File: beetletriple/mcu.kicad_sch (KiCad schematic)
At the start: 14 parts, among them J5 input_c1, J6 input_c2, J7 input_c3, U3 ATtiny1617-M

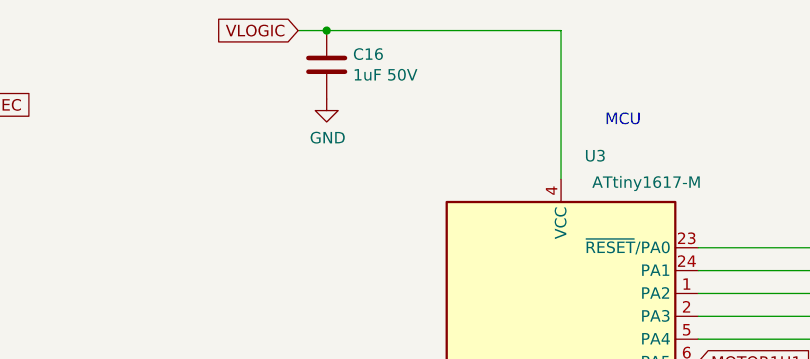
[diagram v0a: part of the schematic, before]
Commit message: Beetleweight triple esc
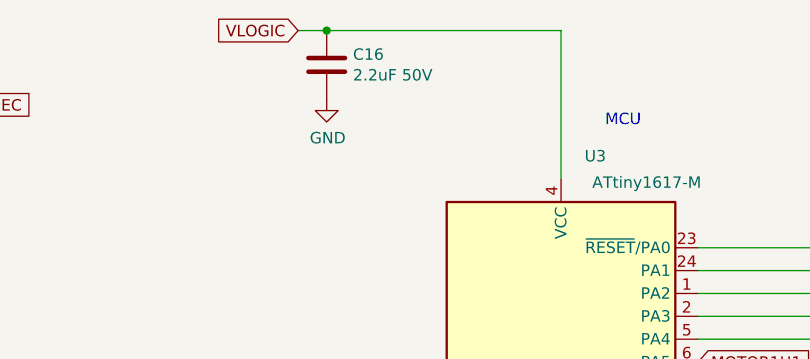
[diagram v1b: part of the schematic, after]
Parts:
- C16: value 1uF 50V -> 2.2uF 50V; LCSC (none) -> C50254
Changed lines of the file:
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@@
       (effects (font (size 1.27 1.27)) (justify left))
     )
-    (property "Value" "1uF 50V" (id 1) (at 106.4261 62.1093 0)
+    (property "Value" "2.2uF 50V" (id 1) (at 106.4261 62.1093 0)
       (effects (font (size 1.27 1.27)) (justify left))
     )
@@
       (effects (font (size 1.27 1.27)) hide)
     )
-    (property "LCSC" "" (id 4) (at 103.505 60.96 0)
+    (property "LCSC" "C50254" (id 4) (at 103.505 60.96 0)
       (effects (font (size 1.27 1.27)) hide)
     )

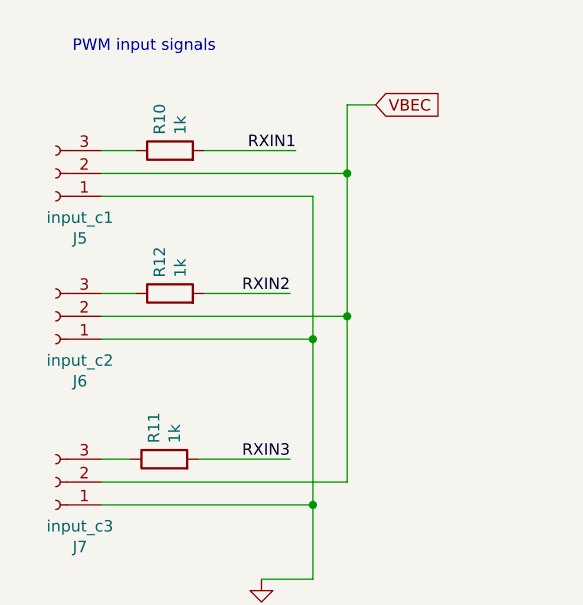
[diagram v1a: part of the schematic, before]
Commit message: Beetleweight triple: redo the power and passives
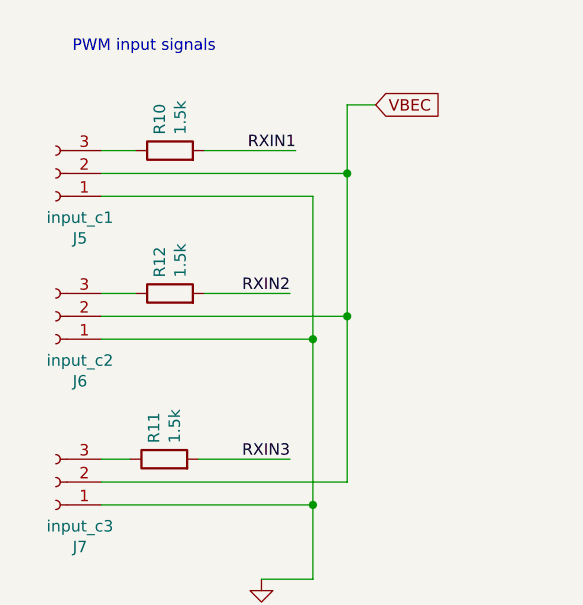
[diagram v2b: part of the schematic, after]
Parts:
- R10, R11, R12: value 1k -> 1.5k
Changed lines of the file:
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@@
       (effects (font (size 1.27 1.27)) (justify left))
     )
-    (property "Value" "1k" (id 1) (at 41.154 102.997 0)
+    (property "Value" "1.5k" (id 1) (at 41.154 102.997 0)
       (effects (font (size 1.27 1.27)) (justify left))
     )
@@
       (effects (font (size 1.27 1.27)) (justify left))
     )
-    (property "Value" "1k" (id 1) (at 41.789 68.707 0)
+    (property "Value" "1.5k" (id 1) (at 41.789 68.707 0)
       (effects (font (size 1.27 1.27)) (justify left))
     )
@@
       (effects (font (size 1.27 1.27)) (justify left))
     )
-    (property "Value" "1k" (id 1) (at 41.789 84.582 0)
+    (property "Value" "1.5k" (id 1) (at 41.789 84.582 0)
       (effects (font (size 1.27 1.27)) (justify left))
     )

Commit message: Beetleweight triple: more.
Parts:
- added J8: output_c4, Connector_PinHeader_2.54mm:PinHeader_1x03_P2.54mm_Vertical, symbol Connector:Conn_01x03_Female
- added J9: output_c5, Connector_PinHeader_2.54mm:PinHeader_1x03_P2.54mm_Vertical, symbol Connector:Conn_01x03_Female
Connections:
- net GND: now also J8.1 (Pin_1), J9.1 (Pin_1)
- net MOTOR1H1: now also U3.11 (PB5); no longer U3.6 (PA5)
- net MOTOR1H2: now also U3.9 (PB7); no longer U3.8 (PA7)
- net MOTOR1L1: now also U3.10 (PB6); no longer U3.7 (PA6)
- net MOTOR1L2: now also U3.8 (PA7); no longer U3.16 (PB0)
- net MOTOR2H1: now also U3.17 (PC0); no longer U3.15 (PB1)
- net MOTOR2H2: now also U3.7 (PA6); no longer U3.13 (PB3)
- net MOTOR2L1: now also U3.16 (PB0); no longer U3.14 (PB2)
- net MOTOR2L2: now also U3.6 (PA5); no longer U3.12 (PB4)
- net MOTOR3H1: now also U3.15 (PB1); no longer U3.11 (PB5)
- net MOTOR3H2: now also U3.13 (PB3); no longer U3.9 (PB7)
- net MOTOR3L1: now also U3.14 (PB2); no longer U3.10 (PB6)
- net MOTOR3L2: now also U3.12 (PB4); no longer U3.17 (PC0)
- net VBEC: now also J8.2 (Pin_2), J9.2 (Pin_2)
- net SERVO2: now reaches U3.19 (PC2)
- net SERVO2: now also J9.3 (Pin_3)
- net SERVO1: now reaches U3.20 (PC3)
- net SERVO1: now also J8.3 (Pin_3)
- no-connect marks 0 -> 1
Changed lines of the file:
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@@
   (junction (at 95.885 168.275) (diameter 0.9144) (color 0 0 0 0))
   (junction (at 103.505 57.15) (diameter 0.9144) (color 0 0 0 0))
+  (junction (at 220.345 116.84) (diameter 0.9144) (color 0 0 0 0))
+  (junction (at 225.425 98.425) (diameter 0.9144) (color 0 0 0 0))
+  (no_connect (at 114.3 106.68))
   (wire (pts (xy 33.02 70.485) (xy 36.83 70.485))
     (stroke (width 0) (type solid) (color 0 0 0 0))
@@
     (stroke (width 0) (type solid) (color 0 0 0 0))
   )
+  (wire (pts (xy 104.14 109.22) (xy 114.3 109.22))
+    (stroke (width 0) (type solid) (color 0 0 0 0))
+  )
+  (wire (pts (xy 104.14 111.76) (xy 114.3 111.76))
+    (stroke (width 0) (type solid) (color 0 0 0 0))
+  )
   (wire (pts (xy 108.585 132.715) (xy 108.585 146.685))
     (stroke (width 0) (type solid) (color 0 0 0 0))
@@
     (stroke (width 0) (type solid) (color 0 0 0 0))
   )
+  (wire (pts (xy 220.345 100.965) (xy 220.345 116.84))
+    (stroke (width 0) (type solid) (color 0 0 0 0))
+  )
+  (wire (pts (xy 220.345 116.84) (xy 220.345 123.19))
+    (stroke (width 0) (type solid) (color 0 0 0 0))
+  )
+  (wire (pts (xy 220.345 116.84) (xy 236.855 116.84))
+    (stroke (width 0) (type solid) (color 0 0 0 0))
+  )
+  (wire (pts (xy 225.425 70.485) (xy 218.44 70.485))
+    (stroke (width 0) (type solid) (color 0 0 0 0))
+  )
+  (wire (pts (xy 225.425 70.485) (xy 225.425 98.425))
+    (stroke (width 0) (type solid) (color 0 0 0 0))
+  )
+  (wire (pts (xy 225.425 98.425) (xy 225.425 114.3))
+    (stroke (width 0) (type solid) (color 0 0 0 0))
+  )
+  (wire (pts (xy 226.695 95.885) (xy 236.855 95.885))
+    (stroke (width 0) (type solid) (color 0 0 0 0))
+  )
+  (wire (pts (xy 228.6 111.76) (xy 236.855 111.76))
+    (stroke (width 0) (type solid) (color 0 0 0 0))
+  )
+  (wire (pts (xy 236.855 98.425) (xy 225.425 98.425))
+    (stroke (width 0) (type solid) (color 0 0 0 0))
+  )
+  (wire (pts (xy 236.855 100.965) (xy 220.345 100.965))
+    (stroke (width 0) (type solid) (color 0 0 0 0))
+  )
+  (wire (pts (xy 236.855 114.3) (xy 225.425 114.3))
+    (stroke (width 0) (type solid) (color 0 0 0 0))
+  )
   (text "PWM input signals" (at 45.72 59.69 180)
     (effects (font (size 1.27 1.27)) (justify right bottom))
@@
     (effects (font (size 1.27 1.27)) (justify left bottom))
   )
+  (label "SERVO2" (at 104.14 109.22 0)
+    (effects (font (size 1.27 1.27)) (justify left bottom))
+  )
+  (label "SERVO1" (at 104.14 111.76 0)
+    (effects (font (size 1.27 1.27)) (justify left bottom))
+  )
   (label "BLINKY2" (at 108.585 144.78 90)
     (effects (font (size 1.27 1.27)) (justify left bottom))
@@
   (label "RXIN3" (at 165.735 91.44 180)
     (effects (font (size 1.27 1.27)) (justify right bottom))
+  )
+  (label "SERVO1" (at 226.695 95.885 0)
+    (effects (font (size 1.27 1.27)) (justify left bottom))
+  )
+  (label "SERVO2" (at 228.6 111.76 0)
+    (effects (font (size 1.27 1.27)) (justify left bottom))
   )
   (global_label "VBEC" (shape input) (at 63.5 65.405 0)
@@
     )
   )
-  (global_label "MOTOR3L2" (shape input) (at 114.3 104.14 180)
+  (global_label "MOTOR2H1" (shape input) (at 114.3 104.14 180)
     (effects (font (size 1.27 1.27)) (justify right))
-    (property "Intersheet References" "${INTERSHEET_REFS}" (id 0) (at 100.5658 104.0606 0)
+    (property "Intersheet References" "${INTERSHEET_REFS}" (id 0) (at 100.2634 104.2194 0)
       (effects (font (size 1.27 1.27)) (justify right) hide)
     )
   )
-  (global_label "MOTOR1H1" (shape input) (at 144.78 93.98 0)
-    (effects (font (size 1.27 1.27)) (justify left))
-    (property "Intersheet References" "${INTERSHEET_REFS}" (id 0) (at 158.8166 93.9006 0)
-      (effects (font (size 1.27 1.27)) (justify left) hide)
-    )
-  )
-  (global_label "MOTOR1L1" (shape input) (at 144.78 96.52 0)
-    (effects (font (size 1.27 1.27)) (justify left))
-    (property "Intersheet References" "${INTERSHEET_REFS}" (id 0) (at 158.5142 96.4406 0)
-      (effects (font (size 1.27 1.27)) (justify left) hide)
-    )
-  )
-  (global_label "MOTOR1H2" (shape input) (at 144.78 99.06 0)
-    (effects (font (size 1.27 1.27)) (justify left))
-    (property "Intersheet References" "${INTERSHEET_REFS}" (id 0) (at 158.8166 98.9806 0)
-      (effects (font (size 1.27 1.27)) (justify left) hide)
-    )
-  )
-  (global_label "MOTOR1L2" (shape input) (at 144.78 104.14 0)
+  (global_label "MOTOR2L2" (shape input) (at 144.78 93.98 0)
+    (effects (font (size 1.27 1.27)) (justify left))
+    (property "Intersheet References" "${INTERSHEET_REFS}" (id 0) (at 158.5142 93.9006 0)
+      (effects (font (size 1.27 1.27)) (justify left) hide)
+    )
+  )
+  (global_label "MOTOR2H2" (shape input) (at 144.78 96.52 0)
+    (effects (font (size 1.27 1.27)) (justify left))
+    (property "Intersheet References" "${INTERSHEET_REFS}" (id 0) (at 158.8166 96.4406 0)
+      (effects (font (size 1.27 1.27)) (justify left) hide)
+    )
+  )
+  (global_label "MOTOR1L2" (shape input) (at 144.78 99.06 0)
+    (effects (font (size 1.27 1.27)) (justify left))
+    (property "Intersheet References" "${INTERSHEET_REFS}" (id 0) (at 158.5142 98.9806 0)
+      (effects (font (size 1.27 1.27)) (justify left) hide)
+    )
+  )
+  (global_label "MOTOR2L1" (shape input) (at 144.78 104.14 0)
     (effects (font (size 1.27 1.27)) (justify left))
     (property "Intersheet References" "${INTERSHEET_REFS}" (id 0) (at 158.5142 104.0606 0)
@@
     )
   )
-  (global_label "MOTOR2H1" (shape input) (at 144.78 106.68 0)
+  (global_label "MOTOR3H1" (shape input) (at 144.78 106.68 0)
     (effects (font (size 1.27 1.27)) (justify left))
     (property "Intersheet References" "${INTERSHEET_REFS}" (id 0) (at 158.8166 106.6006 0)
@@
     )
   )
-  (global_label "MOTOR2L1" (shape input) (at 144.78 109.22 0)
+  (global_label "MOTOR3L1" (shape input) (at 144.78 109.22 0)
     (effects (font (size 1.27 1.27)) (justify left))
     (property "Intersheet References" "${INTERSHEET_REFS}" (id 0) (at 158.5142 109.1406 0)
@@
     )
   )
-  (global_label "MOTOR2H2" (shape input) (at 144.78 111.76 0)
+  (global_label "MOTOR3H2" (shape input) (at 144.78 111.76 0)
     (effects (font (size 1.27 1.27)) (justify left))
     (property "Intersheet References" "${INTERSHEET_REFS}" (id 0) (at 158.8166 111.6806 0)
@@
     )
   )
-  (global_label "MOTOR2L2" (shape input) (at 144.78 114.3 0)
-    (effects (font (size 1.27 1.27)) (justify left))
-    (property "Intersheet References" "${INTERSHEET_REFS}" (id 0) (at 158.5142 114.2206 0)
-      (effects (font (size 1.27 1.27)) (justify left) hide)
-    )
-  )
-  (global_label "MOTOR3H1" (shape input) (at 144.78 116.84 0)
+  (global_label "MOTOR3L2" (shape input) (at 144.78 114.3 0)
+    (effects (font (size 1.27 1.27)) (justify left))
+    (property "Intersheet References" "${INTERSHEET_REFS}" (id 0) (at 158.5142 114.3794 0)
+      (effects (font (size 1.27 1.27)) (justify left) hide)
+    )
+  )
+  (global_label "MOTOR1H1" (shape input) (at 144.78 116.84 0)
     (effects (font (size 1.27 1.27)) (justify left))
     (property "Intersheet References" "${INTERSHEET_REFS}" (id 0) (at 158.8166 116.7606 0)
@@
     )
   )
-  (global_label "MOTOR3L1" (shape input) (at 144.78 119.38 0)
+  (global_label "MOTOR1L1" (shape input) (at 144.78 119.38 0)
     (effects (font (size 1.27 1.27)) (justify left))
     (property "Intersheet References" "${INTERSHEET_REFS}" (id 0) (at 158.5142 119.3006 0)
@@
     )
   )
-  (global_label "MOTOR3H2" (shape input) (at 144.78 121.92 0)
+  (global_label "MOTOR1H2" (shape input) (at 144.78 121.92 0)
     (effects (font (size 1.27 1.27)) (justify left))
     (property "Intersheet References" "${INTERSHEET_REFS}" (id 0) (at 158.8166 121.8406 0)
       (effects (font (size 1.27 1.27)) (justify left) hide)
+    )
+  )
+  (global_label "VBEC" (shape input) (at 218.44 70.485 180)
+    (effects (font (size 1.27 1.27)) (justify right))
+    (property "Intersheet References" "${INTERSHEET_REFS}" (id 0) (at 209.7253 70.4056 0)
+      (effects (font (size 1.27 1.27)) (justify right) hide)
     )
   )
@@
     )
     (property "Datasheet" "" (id 3) (at 129.54 132.715 0)
+      (effects (font (size 1.27 1.27)) hide)
+    )
+    (pin "1")
+  )
+  (symbol (lib_id "power:GND") (at 220.345 123.19 0) (mirror y) (unit 1)
+    (in_bom yes) (on_board yes)
+    (property "Reference" "#PWR020" (id 0) (at 220.345 129.54 0)
+      (effects (font (size 1.27 1.27)) hide)
+    )
+    (property "Value" "GND" (id 1) (at 220.2307 127.5144 0))
+    (property "Footprint" "" (id 2) (at 220.345 123.19 0)
+      (effects (font (size 1.27 1.27)) hide)
+    )
+    (property "Datasheet" "" (id 3) (at 220.345 123.19 0)
       (effects (font (size 1.27 1.27)) hide)
     )
@@
       (effects (font (size 1.27 1.27)) hide)
     )
+    (pin "1")
+    (pin "2")
+    (pin "3")
+  )
+  (symbol (lib_id "Connector:Conn_01x03_Female") (at 241.935 98.425 0) (mirror x) (unit 1)
+    (in_bom yes) (on_board yes)
+    (property "Reference" "J8" (id 0) (at 239.2426 105.6324 0))
+    (property "Value" "output_c4" (id 1) (at 239.243 103.334 0))
+    (property "Footprint" "Connector_PinHeader_2.54mm:PinHeader_1x03_P2.54mm_Vertical" (id 2) (at 241.935 98.425 0)
+      (effects (font (size 1.27 1.27)) hide)
+    )
+    (property "Datasheet" "~" (id 3) (at 241.935 98.425 0)
+      (effects (font (size 1.27 1.27)) hide)
+    )
+    (pin "1")
+    (pin "2")
+    (pin "3")
+  )
+  (symbol (lib_id "Connector:Conn_01x03_Female") (at 241.935 114.3 0) (mirror x) (unit 1)
+    (in_bom yes) (on_board yes)
+    (property "Reference" "J9" (id 0) (at 239.2426 121.5074 0))
+    (property "Value" "output_c5" (id 1) (at 239.243 119.209 0))
+    (property "Footprint" "Connector_PinHeader_2.54mm:PinHeader_1x03_P2.54mm_Vertical" (id 2) (at 241.935 114.3 0)
+      (effects (font (size 1.27 1.27)) hide)
+    )
+    (property "Datasheet" "~" (id 3) (at 241.935 114.3 0)
+      (effects (font (size 1.27 1.27)) hide)
+    )

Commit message: misc updates
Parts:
- added J10: soicbite programming connector, beetletriple:SOIC_clipProgSmall, symbol Connector:Conn_01x08_Male
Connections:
- net BLINKY1: now also R14.2, U3.22 (PC5); no longer D9.2 (A), U3.21 (PC4)
- net BLINKY2: now also R15.2, U3.21 (PC4); no longer D10.2 (A), U3.22 (PC5)
- net GND: now also D10.1 (K), D8.1 (K), D9.1 (K), J10.3 (Pin_3); no longer R13.1, R14.1, R15.1
- net TXDEBUG: now also J10.8 (Pin_8)
- net UPDI: now also J10.6 (Pin_6)
- net VLOGIC: now also R13.2, J10.1 (Pin_1); no longer D8.2 (A)
- new net: D9.2 (A), R14.1
- new net: D10.2 (A), R15.1
- new net: D8.2 (A), R13.1
- no-connect marks 1 -> 5
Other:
- moved on the sheet: D10, D8, D9, R13, R14, R15

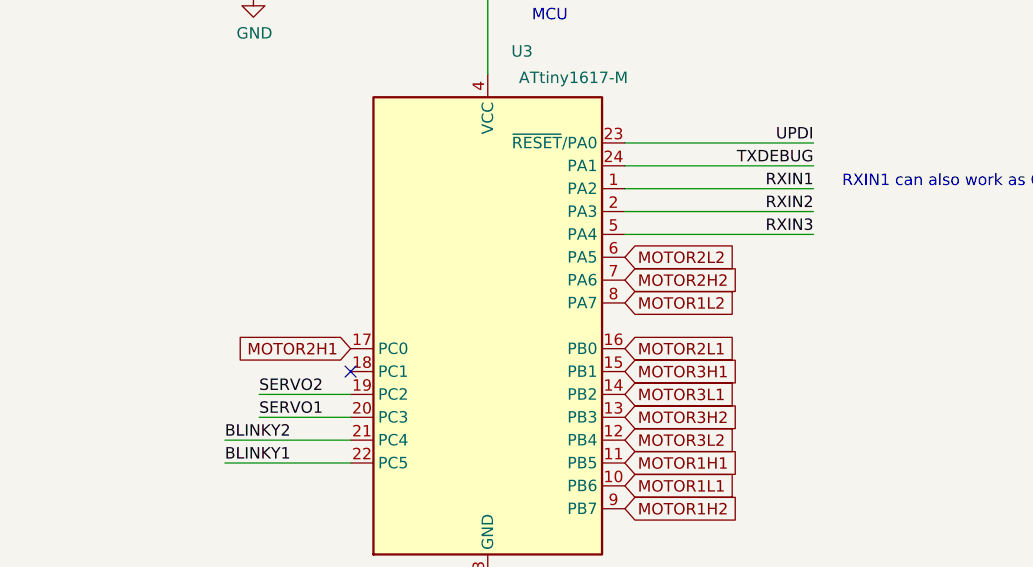
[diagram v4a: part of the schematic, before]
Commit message: Shunt current sensor. Many improvements, layout updates
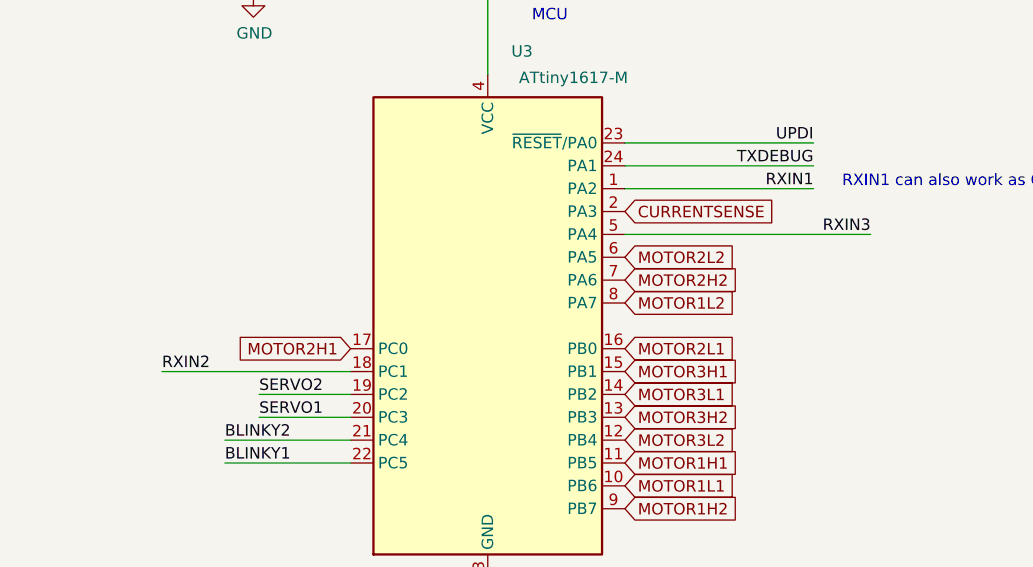
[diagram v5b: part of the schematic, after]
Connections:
- net RXIN2: now also U3.18 (PC1); no longer U3.2 (PA3)
- new net CURRENTSENSE: U3.2 (PA3)
- no-connect marks 5 -> 4
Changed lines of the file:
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@@
   (junction (at 220.345 116.84) (diameter 0.9144) (color 0 0 0 0))
   (junction (at 225.425 98.425) (diameter 0.9144) (color 0 0 0 0))
-  (no_connect (at 114.3 106.68))
   (no_connect (at 213.36 41.91))
   (no_connect (at 213.36 46.99))
@@
     (stroke (width 0) (type solid) (color 0 0 0 0))
   )
+  (wire (pts (xy 114.3 106.68) (xy 93.345 106.68))
+    (stroke (width 0) (type solid) (color 0 0 0 0))
+  )
   (wire (pts (xy 129.54 57.15) (xy 129.54 73.66))
     (stroke (width 0) (type solid) (color 0 0 0 0))
@@
     (stroke (width 0) (type solid) (color 0 0 0 0))
   )
-  (wire (pts (xy 144.78 88.9) (xy 165.735 88.9))
-    (stroke (width 0) (type solid) (color 0 0 0 0))
-  )
-  (wire (pts (xy 144.78 91.44) (xy 165.735 91.44))
+  (wire (pts (xy 144.78 91.44) (xy 172.085 91.44))
     (stroke (width 0) (type solid) (color 0 0 0 0))
   )
@@
     (effects (font (size 1.27 1.27)) (justify right bottom))
   )
+  (label "RXIN2" (at 93.345 106.68 0)
+    (effects (font (size 1.27 1.27)) (justify left bottom))
+  )
   (label "BLINKY1" (at 95.885 144.78 90)
     (effects (font (size 1.27 1.27)) (justify left bottom))
@@
     (effects (font (size 1.27 1.27)) (justify right bottom))
   )
-  (label "RXIN2" (at 165.735 88.9 180)
-    (effects (font (size 1.27 1.27)) (justify right bottom))
-  )
-  (label "RXIN3" (at 165.735 91.44 180)
+  (label "RXIN3" (at 172.085 91.44 180)
     (effects (font (size 1.27 1.27)) (justify right bottom))
   )
@@
     )
   )
+  (global_label "CURRENTSENSE" (shape input) (at 144.78 88.9 0)
+    (effects (font (size 1.27 1.27)) (justify left))
+    (property "Intersheet References" "${INTERSHEET_REFS}" (id 0) (at 163.3523 88.8206 0)
+      (effects (font (size 1.27 1.27)) (justify left) hide)
+    )
+  )
